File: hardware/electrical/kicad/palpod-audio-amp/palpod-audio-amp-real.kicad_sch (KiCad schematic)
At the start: 73 parts, among them J1 PSU_INPUT, J2 I2S_DSD_IN, J24 SPKR_TWEETER, J25 SPKR_MID, J26 SPKR_WOOFER, J27 SPKR_SUBWOOFER, U10 THAT1512_MID, U11 THAT1512_WOOFER, U12 THAT1512_SUBWOOFER, U17 LM5116MHX_PLUS60V, U18 LM5116MHX_MINUS60V, U19 TPS3808G01DBVR, U20 ADT7420_TWEETER, U21 ADT7420_MID, U22 ADT7420_WOOFER, U23 ADT7420_SUBWOOFER, U3 CS2100-CP, U4 Si8660BB-B-IS1, U5 CS43198_TWEETER, U6 CS43198_MID, U7 CS43198_WOOFER, U8 CS43198_SUBWOOFER, U9 THAT1512_TWEETER

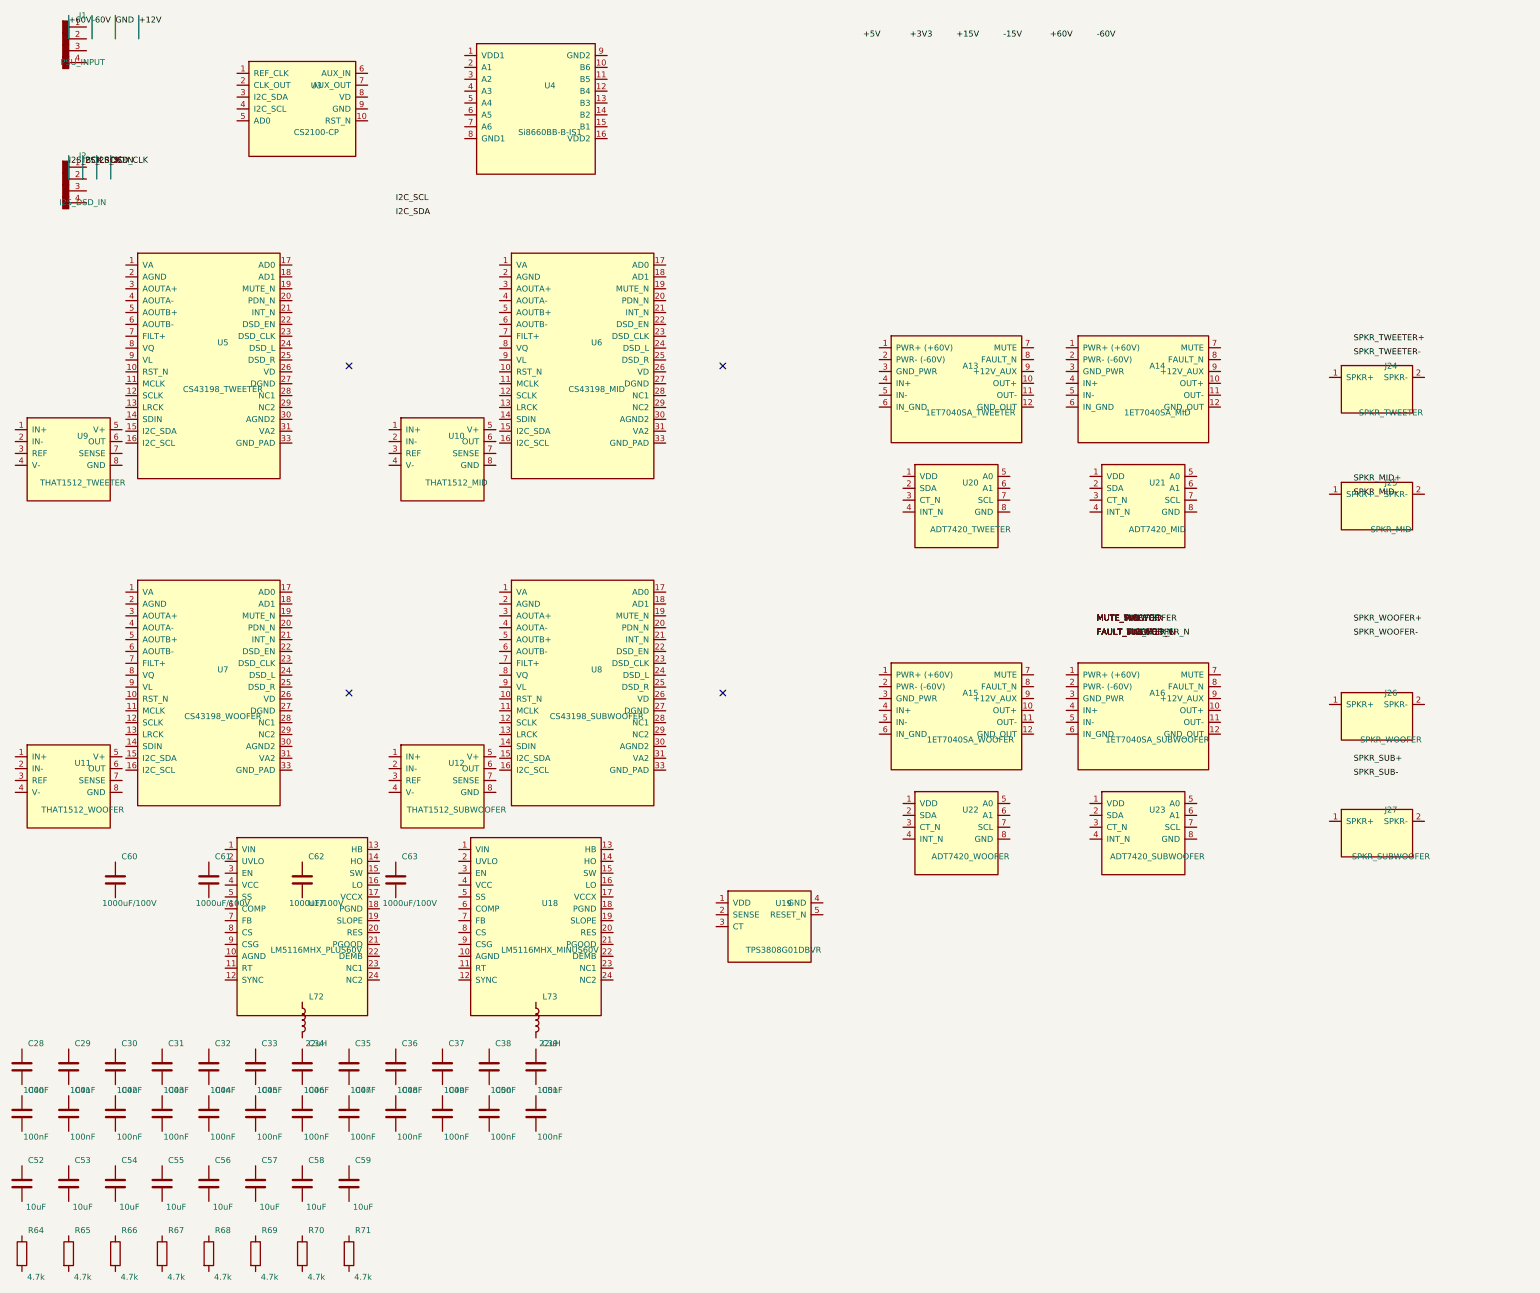
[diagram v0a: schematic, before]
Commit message: ci: Loosen cosmetic lint rules + fix substantive shellcheck warnings
Config:
- .markdownlint.jsonc: disable MD013/024/025/033/040/041/049 (noise
  on long prose files, table headings, badges, code fence language,
  emphasis-style mismatch from generated content)
- .yamllint.yaml: relax colons/braces spacing (GitHub Actions style),
  disable line-length + document-start + truthy-check-keys
- ruff.toml: ignore E702 (multi-statement lines used in table-format
  parse scripts), E501 line-length, E731 lambda

Source fixes:
- scripts/media-import.sh: quote MODE="link" etc (SC2209)
- All source .env lines: add shellcheck disable comment (source is
  runtime env, not lint-time file to follow)

Substantive checks still active:
- ruff catches real bugs (undefined names, unused imports)
- shellcheck catches real quoting/expansion issues
- markdownlint catches broken links, missing alt text
- yamllint catches malformed YAML structure
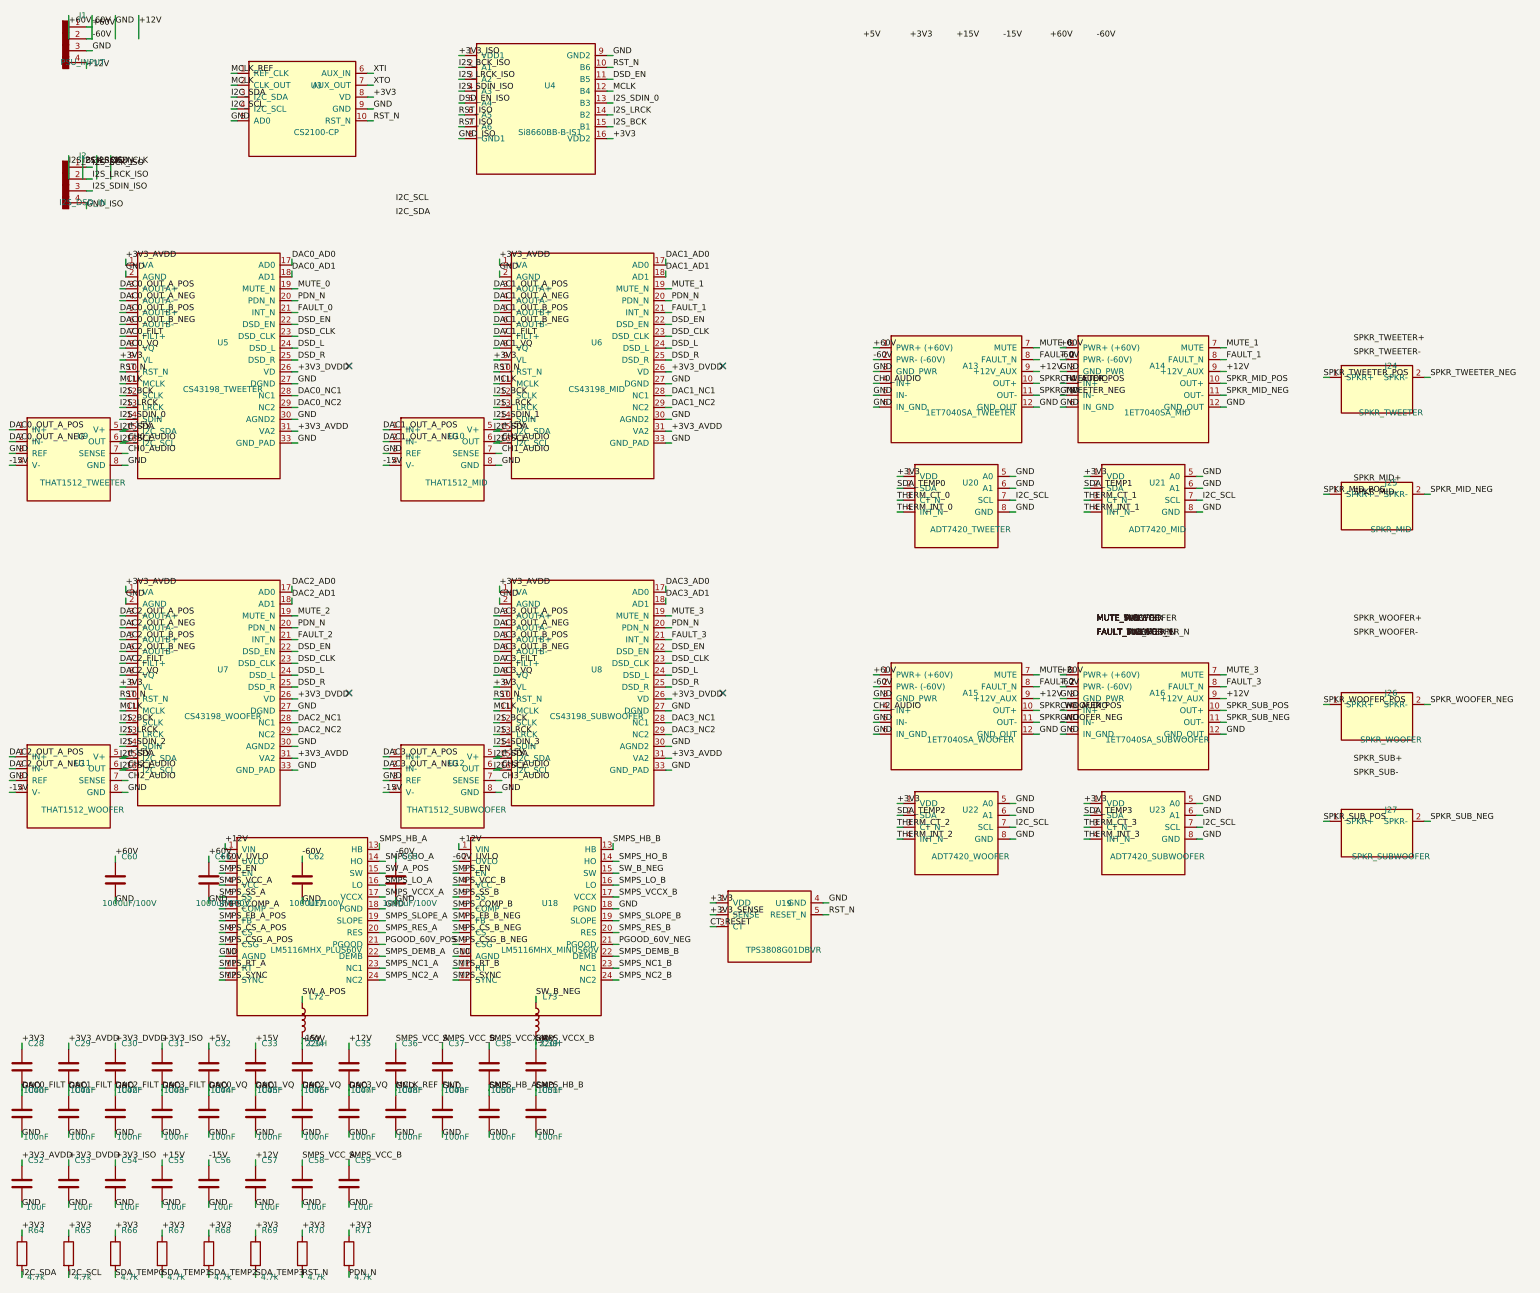
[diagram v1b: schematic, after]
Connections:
- net +12V: now also A13.9 (+12V_AUX), A14.9 (+12V_AUX), A15.9 (+12V_AUX), A16.9 (+12V_AUX), C35.1, C57.1, J1.4 (Pin_4), U17.1 (VIN), U18.1 (VIN)
- net +15V: now also C33.1, C55.1, U10.5 (V+), U11.5 (V+), U12.5 (V+), U9.5 (V+)
- net +3V3: now also C28.1, R64.1, R65.1, R66.1, R67.1, R68.1, R69.1, R70.1, R71.1, U19.1 (VDD), U20.1 (VDD), U21.1 (VDD), U22.1 (VDD), U23.1 (VDD), U3.8 (VD), U4.16 (VDD2), U5.9 (VL), U6.9 (VL), U7.9 (VL), U8.9 (VL)
- net +5V: now also C32.1
- net +60V: now also A13.1 (PWR+ (+60V)), A14.1 (PWR+ (+60V)), A15.1 (PWR+ (+60V)), A16.1 (PWR+ (+60V)), C34.1, C56.1, C60.1, C61.1, J1.1 (Pin_1), L72.2, U10.4 (V-), U11.4 (V-), U12.4 (V-), U9.4 (V-)
- net -60V: now also A13.2 (PWR- (-60V)), A14.2 (PWR- (-60V)), A15.2 (PWR- (-60V)), A16.2 (PWR- (-60V)), C39.1, C62.1, C63.1, J1.2 (Pin_2), L73.2, U18.17 (VCCX)
- net DSD_CLK: now also U5.23 (DSD_CLK), U6.23 (DSD_CLK), U7.23 (DSD_CLK), U8.23 (DSD_CLK)
- net I2C_SCL: now also R65.2, U20.7 (SCL), U21.7 (SCL), U22.7 (SCL), U23.7 (SCL), U3.4 (I2C_SCL), U5.16 (I2C_SCL), U6.16 (I2C_SCL), U7.16 (I2C_SCL), U8.16 (I2C_SCL)
- net I2C_SDA: now also R64.2, U3.3 (I2C_SDA), U5.15 (I2C_SDA), U6.15 (I2C_SDA), U7.15 (I2C_SDA), U8.15 (I2C_SDA)
- net I2S_BCK: now also U4.15 (B1), U5.12 (SCLK), U6.12 (SCLK), U7.12 (SCLK), U8.12 (SCLK)
- net I2S_LRCK: now also U4.14 (B2), U5.13 (LRCK), U6.13 (LRCK), U7.13 (LRCK), U8.13 (LRCK)
- net SPKR_MID_POS: now reaches J25.1 (SPKR+)
- net SPKR_MID_POS: now also A14.10 (OUT+)
- net SPKR_MID_NEG: now reaches J25.2 (SPKR-)
- net SPKR_MID_NEG: now also A14.11 (OUT-)
- net DAC0_FILT: now reaches C41.1
- net DAC0_FILT: now also A13.12 (GND_OUT), A13.3 (GND_PWR), A13.5 (IN-), A13.6 (IN_GND), A14.12 (GND_OUT), A14.3 (GND_PWR), A14.5 (IN-), A14.6 (IN_GND), A15.12 (GND_OUT), A15.3 (GND_PWR), A15.5 (IN-), A15.6 (IN_GND), A16.12 (GND_OUT), A16.3 (GND_PWR), A16.5 (IN-), A16.6 (IN_GND), C28.2, C29.2, C30.2, C31.2, C32.2, C33.2, C34.2, C35.2, C36.2, C37.2, C38.2, C39.2, C40.1, C40.2, C41.2, C42.1, C42.2, C43.1, C43.2, C44.1, C44.2, C45.1, C45.2, C46.1, C46.2, C47.1, C47.2, C48.1, C48.2, C49.1, C49.2, C50.1, C50.2, C51.1, C51.2, C52.2, C53.2, C54.2, C55.2, C56.2, C57.2, C58.2, C59.2, C60.2, C61.2, C62.2, C63.2, J1.3 (Pin_3), U10.3 (REF), U10.8 (GND), U11.3 (REF), U11.8 (GND), U12.3 (REF), U12.8 (GND), U17.10 (AGND), U17.13 (HB), U17.18 (PGND), U18.10 (AGND), U18.13 (HB), U18.18 (PGND), U19.4 (GND), U20.5 (A0), U20.6 (A1), U20.8 (GND), U21.5 (A0), U21.6 (A1), U21.8 (GND), U22.5 (A0), U22.6 (A1), U22.8 (GND), U23.5 (A0), U23.6 (A1), U23.8 (GND), U3.1 (REF_CLK), U3.5 (AD0), U3.9 (GND), U4.9 (GND2), U5.2 (AGND), U5.27 (DGND), U5.30 (AGND2), U5.33 (GND_PAD), U5.7 (FILT+), U5.8 (VQ), U6.2 (AGND), U6.27 (DGND), U6.30 (AGND2), U6.33 (GND_PAD), U6.7 (FILT+), U6.8 (VQ), U7.2 (AGND), U7.27 (DGND), U7.30 (AGND2), U7.33 (GND_PAD), U7.7 (FILT+), U7.8 (VQ), U8.2 (AGND), U8.27 (DGND), U8.30 (AGND2), U8.33 (GND_PAD), U8.7 (FILT+), U8.8 (VQ), U9.3 (REF), U9.8 (GND)
- net SDA_TEMP3: now reaches R69.2
- net SDA_TEMP3: now also U23.2 (SDA)
- net +3V3_AVDD: now reaches U6.1 (VA)
- net +3V3_AVDD: now also C29.1, C52.1, U5.1 (VA), U5.31 (VA2), U6.31 (VA2), U7.1 (VA), U7.31 (VA2), U8.1 (VA), U8.31 (VA2)
- net RST_N: now reaches U6.10 (RST_N)
- net RST_N: now also R70.2, U19.5 (RESET_N), U3.10 (RST_N), U4.10 (B6), U5.10 (RST_N), U7.10 (RST_N), U8.10 (RST_N)
- net MCLK: now reaches U6.11 (MCLK)
- net MCLK: now also U3.2 (CLK_OUT), U4.12 (B4), U5.11 (MCLK), U7.11 (MCLK), U8.11 (MCLK)
- net I2S_SDIN_1: now reaches U6.14 (SDIN)
- net DAC1_AD0: now reaches U6.17 (AD0)
- net DAC1_AD1: now reaches U6.18 (AD1)
- net MUTE_1: now reaches U6.19 (MUTE_N)
- net MUTE_1: now also A14.7 (MUTE)
- net PDN_N: now reaches U6.20 (PDN_N)
- net PDN_N: now also R71.2, U5.20 (PDN_N), U7.20 (PDN_N), U8.20 (PDN_N)
- net FAULT_1: now reaches U6.21 (INT_N)
- net FAULT_1: now also A14.8 (FAULT_N)
- net DSD_EN: now reaches U6.22 (DSD_EN)
- net DSD_EN: now also U4.11 (B5), U5.22 (DSD_EN), U7.22 (DSD_EN), U8.22 (DSD_EN)
- net DSD_L: now reaches U6.24 (DSD_L)
- net DSD_L: now also U5.24 (DSD_L), U7.24 (DSD_L), U8.24 (DSD_L)
- net DSD_R: now reaches U6.25 (DSD_R)
- net DSD_R: now also U5.25 (DSD_R), U7.25 (DSD_R), U8.25 (DSD_R)
- net +3V3_DVDD: now reaches U6.26 (VD)
- net +3V3_DVDD: now also C30.1, C53.1, U5.26 (VD), U7.26 (VD), U8.26 (VD)
- net DAC1_NC1: now reaches U6.28 (NC1)
- net DAC1_NC2: now reaches U6.29 (NC2)
- net DAC1_OUT_A_POS: now reaches U6.3 (AOUTA+)
- net DAC1_OUT_A_POS: now also U10.1 (IN+)
- net DAC1_OUT_A_NEG: now reaches U6.4 (AOUTA-)
- net DAC1_OUT_A_NEG: now also U10.2 (IN-)
- net DAC1_OUT_B_POS: now reaches U6.5 (AOUTB+)
- net DAC1_OUT_B_NEG: now reaches U6.6 (AOUTB-)
- net +3V3_ISO: now reaches U4.1 (VDD1)
- net +3V3_ISO: now also C31.1, C54.1
- net I2S_SDIN_0: now reaches U4.13 (B3)
- net I2S_SDIN_0: now also U5.14 (SDIN)
- net I2S_BCK_ISO: now reaches U4.2 (A1)
- net I2S_BCK_ISO: now also J2.1 (Pin_1)
- net I2S_LRCK_ISO: now reaches U4.3 (A2)
- net I2S_LRCK_ISO: now also J2.2 (Pin_2)
- net I2S_SDIN_ISO: now reaches U4.4 (A3)
- net I2S_SDIN_ISO: now also J2.3 (Pin_3)
- net DSD_EN_ISO: now reaches U4.5 (A4)
- net RST_ISO: now reaches U4.6 (A5)
- net RST_ISO: now also U4.7 (A6)
- net GND_ISO: now reaches U4.8 (GND1)
- net GND_ISO: now also J2.4 (Pin_4)
- net SPKR_WOOFER_POS: now reaches A15.10 (OUT+)
- net SPKR_WOOFER_POS: now also J26.1 (SPKR+)
- net SPKR_WOOFER_NEG: now reaches A15.11 (OUT-)
- net SPKR_WOOFER_NEG: now also J26.2 (SPKR-)
- net CH2_AUDIO: now reaches A15.4 (IN+)
- net CH2_AUDIO: now also U11.6 (OUT), U11.7 (SENSE)
- net MUTE_2: now reaches A15.7 (MUTE)
- net MUTE_2: now also U7.19 (MUTE_N)
- net FAULT_2: now reaches A15.8 (FAULT_N)
- net FAULT_2: now also U7.21 (INT_N)
- net SDA_TEMP0: now reaches R66.2
- net SDA_TEMP0: now also U20.2 (SDA)
- net SMPS_RT_B: now reaches U18.11 (RT)
- net SMPS_SYNC: now reaches U18.12 (SYNC)
- net SMPS_SYNC: now also U17.12 (SYNC)
- net SMPS_HO_B: now reaches U18.14 (HO)
- net SW_B_NEG: now reaches U18.15 (SW)
- net SW_B_NEG: now also L73.1
- net SMPS_LO_B: now reaches U18.16 (LO)
- net SMPS_SLOPE_B: now reaches U18.19 (SLOPE)
- net -60V_UVLO: now reaches U18.2 (UVLO)
- net SMPS_RES_B: now reaches U18.20 (RES)
- net PGOOD_60V_NEG: now reaches U18.21 (PGOOD)
- net SMPS_DEMB_B: now reaches U18.22 (DEMB)
- net SMPS_NC1_B: now reaches U18.23 (NC1)
- net SMPS_NC2_B: now reaches U18.24 (NC2)
- net SMPS_EN: now reaches U18.3 (EN)
- net SMPS_EN: now also U17.3 (EN)
- net SMPS_VCC_B: now reaches U18.4 (VCC)
- net SMPS_VCC_B: now also C37.1, C59.1
- net SMPS_SS_B: now reaches U18.5 (SS)
- net SMPS_COMP_B: now reaches U18.6 (COMP)
- net SMPS_FB_B_NEG: now reaches U18.7 (FB)
- net SMPS_CS_B_NEG: now reaches U18.8 (CS)
- net SMPS_CSG_B_NEG: now reaches U18.9 (CSG)
- net SDA_TEMP2: now reaches U22.2 (SDA)
- net SDA_TEMP2: now also R68.2
- net THERM_CT_2: now reaches U22.3 (CT_N)
- net THERM_INT_2: now reaches U22.4 (INT_N)
- net SW_A_POS: now reaches L72.1
- net SW_A_POS: now also U17.15 (SW)
- net DAC2_OUT_A_POS: now reaches U11.1 (IN+)
- net DAC2_OUT_A_POS: now also U7.3 (AOUTA+)
- net DAC2_OUT_A_NEG: now reaches U11.2 (IN-)
- net DAC2_OUT_A_NEG: now also U7.4 (AOUTA-)
- net SDA_TEMP1: now reaches R67.2
- net SDA_TEMP1: now also U21.2 (SDA)
- net SPKR_SUB_POS: now reaches A16.10 (OUT+)
- net SPKR_SUB_POS: now also J27.1 (SPKR+)
- net SPKR_SUB_NEG: now reaches A16.11 (OUT-)
- net SPKR_SUB_NEG: now also J27.2 (SPKR-)
- net CH3_AUDIO: now reaches A16.4 (IN+)
- net CH3_AUDIO: now also U12.6 (OUT), U12.7 (SENSE)
- net MUTE_3: now reaches A16.7 (MUTE)
- net MUTE_3: now also U8.19 (MUTE_N)
- net FAULT_3: now reaches A16.8 (FAULT_N)
- net FAULT_3: now also U8.21 (INT_N)
- net SMPS_VCC_A: now reaches C36.1
- net SMPS_VCC_A: now also C58.1, U17.4 (VCC)
- net +3V3_SENSE: now reaches U19.2 (SENSE)
- net CT_RESET: now reaches U19.3 (CT)
- net SMPS_RT_A: now reaches U17.11 (RT)
- net SMPS_HO_A: now reaches U17.14 (HO)
- net SMPS_LO_A: now reaches U17.16 (LO)
- net SMPS_VCCX_A: now reaches U17.17 (VCCX)
- net SMPS_VCCX_A: now also C38.1
- net SMPS_SLOPE_A: now reaches U17.19 (SLOPE)
- net +60V_UVLO: now reaches U17.2 (UVLO)
- net SMPS_RES_A: now reaches U17.20 (RES)
- net PGOOD_60V_POS: now reaches U17.21 (PGOOD)
- net SMPS_DEMB_A: now reaches U17.22 (DEMB)
- net SMPS_NC1_A: now reaches U17.23 (NC1)
- net SMPS_NC2_A: now reaches U17.24 (NC2)
- net SMPS_SS_A: now reaches U17.5 (SS)
- net SMPS_COMP_A: now reaches U17.6 (COMP)
- net SMPS_FB_A_POS: now reaches U17.7 (FB)
- net SMPS_CS_A_POS: now reaches U17.8 (CS)
- net SMPS_CSG_A_POS: now reaches U17.9 (CSG)
- net I2S_SDIN_2: now reaches U7.14 (SDIN)
- net DAC2_AD0: now reaches U7.17 (AD0)
- net DAC2_AD1: now reaches U7.18 (AD1)
- net DAC2_NC1: now reaches U7.28 (NC1)
- net DAC2_NC2: now reaches U7.29 (NC2)
- net DAC2_OUT_B_POS: now reaches U7.5 (AOUTB+)
- net DAC2_OUT_B_NEG: now reaches U7.6 (AOUTB-)
- net DAC0_OUT_A_POS: now reaches U9.1 (IN+)
- net DAC0_OUT_A_POS: now also U5.3 (AOUTA+)
- net DAC0_OUT_A_NEG: now reaches U9.2 (IN-)
- net DAC0_OUT_A_NEG: now also U5.4 (AOUTA-)
- net CH0_AUDIO: now reaches U9.6 (OUT)
- net CH0_AUDIO: now also A13.4 (IN+), U9.7 (SENSE)
- net SPKR_TWEETER_POS: now reaches A13.10 (OUT+)
- net SPKR_TWEETER_POS: now also J24.1 (SPKR+)
- net SPKR_TWEETER_NEG: now reaches A13.11 (OUT-)
- net SPKR_TWEETER_NEG: now also J24.2 (SPKR-)
- net MUTE_0: now reaches A13.7 (MUTE)
- net MUTE_0: now also U5.19 (MUTE_N)
- net FAULT_0: now reaches A13.8 (FAULT_N)
- net FAULT_0: now also U5.21 (INT_N)
- net DAC0_AD0: now reaches U5.17 (AD0)
- net DAC0_AD1: now reaches U5.18 (AD1)
- net DAC0_NC1: now reaches U5.28 (NC1)
- net DAC0_NC2: now reaches U5.29 (NC2)
- net DAC0_OUT_B_POS: now reaches U5.5 (AOUTB+)
- net DAC0_OUT_B_NEG: now reaches U5.6 (AOUTB-)
- net THERM_CT_1: now reaches U21.3 (CT_N)
- net THERM_INT_1: now reaches U21.4 (INT_N)
- net THERM_CT_0: now reaches U20.3 (CT_N)
- net THERM_INT_0: now reaches U20.4 (INT_N)
- net THERM_CT_3: now reaches U23.3 (CT_N)
- net THERM_INT_3: now reaches U23.4 (INT_N)
- net CH1_AUDIO: now reaches U10.6 (OUT)
- net CH1_AUDIO: now also A14.4 (IN+), U10.7 (SENSE)
- net XTI: now reaches U3.6 (AUX_IN)
- net XTO: now reaches U3.7 (AUX_OUT)
- net I2S_SDIN_3: now reaches U8.14 (SDIN)
- net DAC3_AD0: now reaches U8.17 (AD0)
- net DAC3_AD1: now reaches U8.18 (AD1)
- net DAC3_NC1: now reaches U8.28 (NC1)
- net DAC3_NC2: now reaches U8.29 (NC2)
- net DAC3_OUT_A_POS: now reaches U8.3 (AOUTA+)
- net DAC3_OUT_A_POS: now also U12.1 (IN+)
- net DAC3_OUT_A_NEG: now reaches U8.4 (AOUTA-)
- net DAC3_OUT_A_NEG: now also U12.2 (IN-)
- net DAC3_OUT_B_POS: now reaches U8.5 (AOUTB+)
- net DAC3_OUT_B_NEG: now reaches U8.6 (AOUTB-)
